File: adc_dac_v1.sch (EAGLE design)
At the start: 349 parts, among them IC1 OPA1662, IC2 ADA4610-2, IC3 ADA4610-2, IC4 OPA1662, IC5 ADA4610-2, IC6 OPA1662, IC7 ADA4610-2, IC8 OPA1662, J1 PJ-202AH, J2 PJ-002B, J3 2-406541-3, P1 M-2X06-87759_M, P2 M-2X10-87759_M, Q1 MMBF4117, U1 AD7960BCPZ-RL7, U10 UA78M05CDCYR, U11 LP5907MFX-1.8/NOPB, U12 ADP2300AUJZ-R7, U13 LM317LIPKG3, U14 LM317LIPKG3, U15 LM337LMX/NOPB, U16 ADR395AUJZ-REEL7, U17 MAX5802, U18 LM337LMX/NOPB, U19 MAX6070BAUT21+T, U2 AD5453, U20 CD40106BM96, U21 ADA4932-1YCPZ-R7, U22 AD7960BCPZ-RL7, U23 BC857BS-13-F, U24 BC857BS-13-F, U25 ADA4932-1YCPZ-R7, U26 AD7960BCPZ-RL7, U27 ADA4932-1YCPZ-R7, U28 AD7960BCPZ-RL7, U29 AD5453YRMZ-REEL7, U3 ADA4932-1YCPZ-R7, U30 AD5453, U31 BC857BS-13-F, U32 AD5453, U33 INA199C2DCKT, U34 INA199C2DCKT, U36 AD8244BRMZ, U4 NLSX3018DTR2G, U5 NLSX3018DTR2G, U6 ADS7952SRHBT, U7 OPA202, U8 REF5025AIDR, U9 ADP150AUJZ-3.3-R7, X1 BU-SMA-G, X2 BU-SMA-G, X3 BU-SMA-G, X4 BU-SMA-G, X5 BU-SMA-G, X6 BU-SMA-G, X7 BU-SMA-G, X8 BU-SMA-G, X9 1365-10

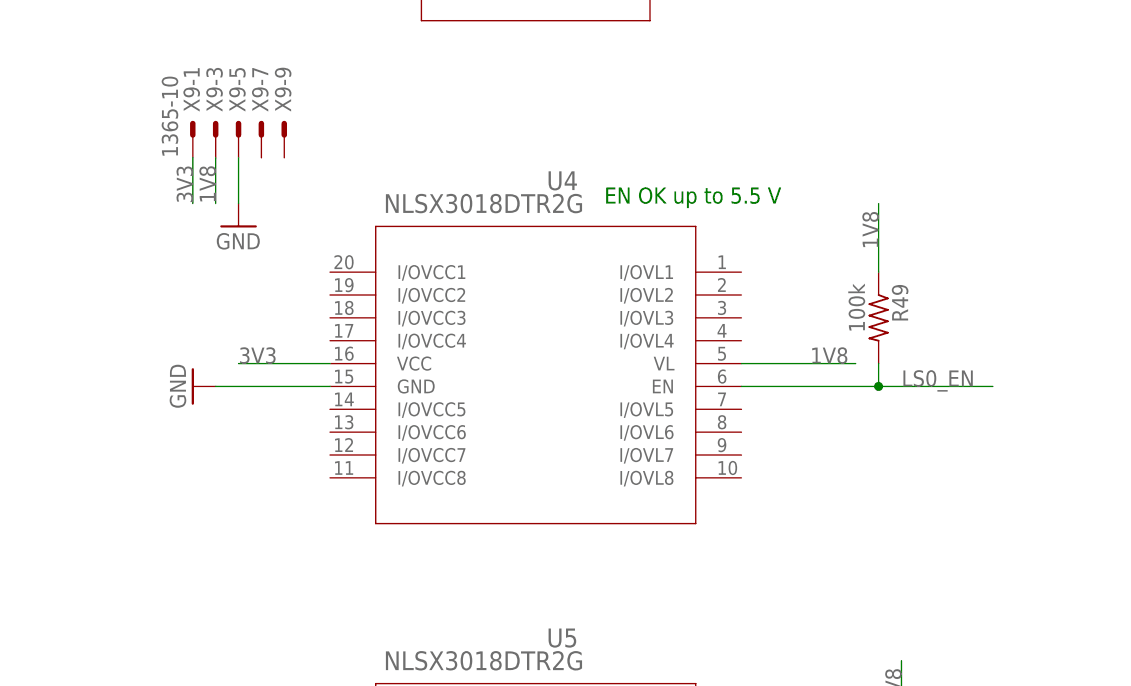
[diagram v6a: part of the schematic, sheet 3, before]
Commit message: placed series terminating resistors
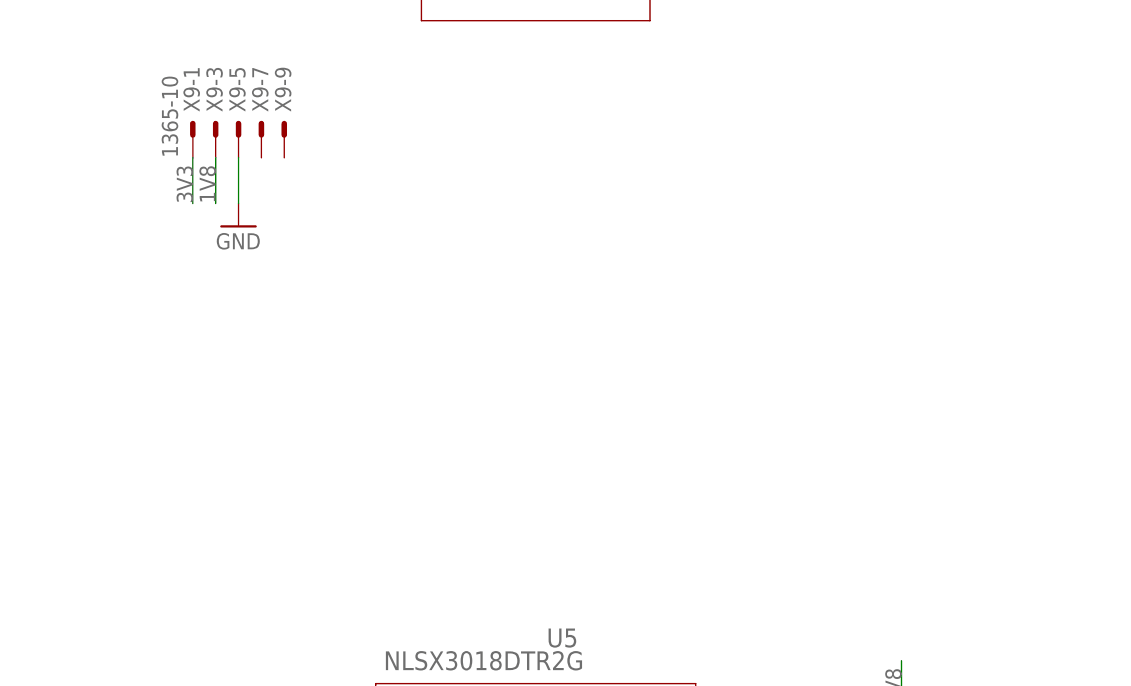
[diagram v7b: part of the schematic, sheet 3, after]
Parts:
- removed R138: 33, rcl:R-US_R0603
- removed R151, R152: DNP, rcl:R-US_R0603
- removed R49: 100k, rcl:R-US_R0603
- removed U4: NLSX3018DTR2G, open_covg:NLSX3018DTR2G
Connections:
- new net N$55: R134.2, U6.SDO
- net 1V8: no longer R49.1, U4.VL
- net 3V3: no longer U4.VCC
- net ADCS_SDO: no longer R134.2, U6.SDO
- net GND: no longer U4.GND
- net LS0_EN: no longer R49.2, U4.EN
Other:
- note removed: "EN OK up to 5.5 V"
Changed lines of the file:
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@@
 <part name="R47" library="rcl" library_urn="urn:adsk.eagle:library:334" deviceset="R-US_" device="R0603" package3d_urn="urn:adsk.eagle:package:23555/3" value="0"/>
 <part name="R48" library="rcl" library_urn="urn:adsk.eagle:library:334" deviceset="R-US_" device="R0603" package3d_urn="urn:adsk.eagle:package:23555/3" value="0"/>
-<part name="GND75" library="supply1" library_urn="urn:adsk.eagle:library:371" deviceset="GND" device=""/>
-<part name="R49" library="rcl" library_urn="urn:adsk.eagle:library:334" deviceset="R-US_" device="R0603" package3d_urn="urn:adsk.eagle:package:23555/3" value="100k"/>
 <part name="R50" library="rcl" library_urn="urn:adsk.eagle:library:334" deviceset="R-US_" device="R0603" package3d_urn="urn:adsk.eagle:package:23555/3" value="100k"/>
 <part name="GND76" library="supply1" library_urn="urn:adsk.eagle:library:371" deviceset="GND" device=""/>
@@
 <part name="U31" library="open_covg" deviceset="HN1A01FU-YLFCT" device="" value="BC857BS-13-F"/>
 <part name="U20" library="open_covg" deviceset="CD40106BM96" device=""/>
-<part name="U4" library="open_covg" deviceset="NLSX3018DTR2G" device=""/>
 <part name="U5" library="open_covg" deviceset="NLSX3018DTR2G" device=""/>
 <part name="U19" library="open_covg" deviceset="MAX6070BAUT21+T" device=""/>
@@
 <part name="R136" library="rcl" library_urn="urn:adsk.eagle:library:334" deviceset="R-US_" device="R0603" package3d_urn="urn:adsk.eagle:package:23555/3" value="33"/>
 <part name="R137" library="rcl" library_urn="urn:adsk.eagle:library:334" deviceset="R-US_" device="R0603" package3d_urn="urn:adsk.eagle:package:23555/3" value="33"/>
-<part name="R138" library="rcl" library_urn="urn:adsk.eagle:library:334" deviceset="R-US_" device="R0603" package3d_urn="urn:adsk.eagle:package:23555/3" value="33"/>
 <part name="R139" library="rcl" library_urn="urn:adsk.eagle:library:334" deviceset="R-US_" device="R0603" package3d_urn="urn:adsk.eagle:package:23555/3" value="33"/>
 <part name="R140" library="rcl" library_urn="urn:adsk.eagle:library:334" deviceset="R-US_" device="R0603" package3d_urn="urn:adsk.eagle:package:23555/3" value="33"/>
@@
 <part name="R149" library="rcl" library_urn="urn:adsk.eagle:library:334" deviceset="R-US_" device="R0603" package3d_urn="urn:adsk.eagle:package:23555/3" value="33"/>
 <part name="R150" library="rcl" library_urn="urn:adsk.eagle:library:334" deviceset="R-US_" device="R0603" package3d_urn="urn:adsk.eagle:package:23555/3" value="33"/>
-<part name="R151" library="rcl" library_urn="urn:adsk.eagle:library:334" deviceset="R-US_" device="R0603" package3d_urn="urn:adsk.eagle:package:23555/3" value="DNP"/>
-<part name="R152" library="rcl" library_urn="urn:adsk.eagle:library:334" deviceset="R-US_" device="R0603" package3d_urn="urn:adsk.eagle:package:23555/3" value="DNP"/>
 <part name="R153" library="rcl" library_urn="urn:adsk.eagle:library:334" deviceset="R-US_" device="R0603" package3d_urn="urn:adsk.eagle:package:23555/3" value="4.7k"/>
 <part name="R154" library="rcl" library_urn="urn:adsk.eagle:library:334" deviceset="R-US_" device="R0603" package3d_urn="urn:adsk.eagle:package:23555/3" value="4.7k"/>
@@
 <attribute name="VALUE" x="163.83" y="99.822" size="1.778" layer="96" rot="R180"/>
 </instance>
-<instance part="R138" gate="G$1" x="81.28" y="71.12" smashed="yes" rot="R180">
-<attribute name="NAME" x="85.09" y="69.6214" size="1.778" layer="95" rot="R180"/>
-<attribute name="VALUE" x="85.09" y="74.422" size="1.778" layer="96" rot="R180"/>
-</instance>
-<instance part="R151" gate="G$1" x="152.4" y="40.64" smashed="yes" rot="R90">
-<attribute name="NAME" x="150.9014" y="36.83" size="1.778" layer="95" rot="R90"/>
-<attribute name="VALUE" x="155.702" y="36.83" size="1.778" layer="96" rot="R90"/>
-</instance>
-<instance part="R152" gate="G$1" x="144.78" y="27.94" smashed="yes" rot="R90">
-<attribute name="NAME" x="143.2814" y="24.13" size="1.778" layer="95" rot="R90"/>
-<attribute name="VALUE" x="148.082" y="24.13" size="1.778" layer="96" rot="R90"/>
-</instance>
 </instances>
 <busses>
@@
 <net name="ADCS_SDO" class="0">
 <segment>
-<pinref part="U6" gate="A" pin="SDO"/>
-<wire x1="119.38" y1="101.6" x2="147.32" y2="101.6" width="0.1524" layer="91"/>
-<pinref part="R134" gate="G$1" pin="2"/>
-</segment>
-<segment>
 <wire x1="157.48" y1="101.6" x2="172.72" y2="101.6" width="0.1524" layer="91"/>
 <label x="167.64" y="101.6" size="1.778" layer="95"/>
@@
 <wire x1="165.1" y1="96.52" x2="172.72" y2="96.52" width="0.1524" layer="91"/>
 <label x="167.64" y="96.52" size="1.778" layer="95"/>
+</segment>
+</net>
+<net name="N$55" class="0">
+<segment>
+<pinref part="U6" gate="A" pin="SDO"/>
+<pinref part="R134" gate="G$1" pin="2"/>
+<wire x1="119.38" y1="101.6" x2="147.32" y2="101.6" width="0.1524" layer="91"/>
 </segment>
 </net>
@@
 <sheet>
 <plain>
-<text x="223.52" y="132.08" size="1.778" layer="91">EN OK up to 5.5 V</text>
 <text x="223.52" y="193.04" size="1.778" layer="91">VSS - VDD
 to FET switches on analog board</text>
@@
 <attribute name="DRAWING_NAME" x="190.5" y="19.05" size="2.54" layer="94"/>
 </instance>
-<instance part="GND75" gate="1" x="177.8" y="111.76" smashed="yes" rot="R270">
-<attribute name="VALUE" x="175.26" y="114.3" size="1.778" layer="96" rot="R270"/>
-</instance>
-<instance part="R49" gate="G$1" x="254" y="119.38" smashed="yes" rot="R270">
-<attribute name="NAME" x="255.4986" y="123.19" size="1.778" layer="95" rot="R270"/>
-<attribute name="VALUE" x="250.698" y="123.19" size="1.778" layer="96" rot="R270"/>
-</instance>
 <instance part="R50" gate="G$1" x="256.54" y="68.58" smashed="yes" rot="R270">
 <attribute name="NAME" x="258.0386" y="72.39" size="1.778" layer="95" rot="R270"/>
@@
 <attribute name="NAME" x="211.1756" y="189.4586" size="2.0828" layer="95" ratio="6" rot="SR0"/>
 <attribute name="VALUE" x="210.5406" y="186.9186" size="2.0828" layer="96" ratio="6" rot="SR0"/>
-</instance>
-<instance part="U4" gate="A" x="241.3" y="124.46" smashed="yes" rot="MR0">
-<attribute name="NAME" x="220.6244" y="133.5786" size="2.0828" layer="95" ratio="6" rot="SMR0"/>
-<attribute name="VALUE" x="221.2594" y="131.0386" size="2.0828" layer="96" ratio="6" rot="SMR0"/>
 </instance>
 <instance part="U5" gate="A" x="241.3" y="73.66" smashed="yes" rot="MR0">
@@
 <nets>
 <net name="1V8" class="1">
-<segment>
-<wire x1="238.76" y1="114.3" x2="251.46" y2="114.3" width="0.1524" layer="91"/>
-<label x="246.38" y="114.3" size="1.778" layer="95"/>
-<pinref part="U4" gate="A" pin="VL"/>
-</segment>
-<segment>
-<pinref part="R49" gate="G$1" pin="1"/>
-<wire x1="254" y1="124.46" x2="254" y2="132.08" width="0.1524" layer="91"/>
-<label x="254" y="127" size="1.778" layer="95" rot="R90"/>
-</segment>
 <segment>
 <wire x1="238.76" y1="63.5" x2="251.46" y2="63.5" width="0.1524" layer="91"/>
@@
 <net name="3V3" class="1">
 <segment>
-<wire x1="193.04" y1="114.3" x2="182.88" y2="114.3" width="0.1524" layer="91"/>
-<label x="182.88" y="114.3" size="1.778" layer="95"/>
-<pinref part="U4" gate="A" pin="VCC"/>
-</segment>
-<segment>
 <wire x1="193.04" y1="63.5" x2="182.88" y2="63.5" width="0.1524" layer="91"/>
 <label x="182.88" y="63.5" size="1.778" layer="95"/>
@@
 </net>
 <net name="GND" class="1">
-<segment>
-<pinref part="GND75" gate="1" pin="GND"/>
-<wire x1="180.34" y1="111.76" x2="193.04" y2="111.76" width="0.1524" layer="91"/>
-<pinref part="U4" gate="A" pin="GND"/>
-</segment>
 <segment>
 <pinref part="GND76" gate="1" pin="GND"/>
@@
 </segment>
 </net>
-<net name="LS0_EN" class="0">
-<segment>
-<wire x1="238.76" y1="111.76" x2="254" y2="111.76" width="0.1524" layer="91"/>
-<pinref part="R49" gate="G$1" pin="2"/>
-<wire x1="254" y1="114.3" x2="254" y2="111.76" width="0.1524" layer="91"/>
-<wire x1="254" y1="111.76" x2="266.7" y2="111.76" width="0.1524" layer="91"/>
-<junction x="254" y="111.76"/>
-<label x="256.54" y="111.76" size="1.778" layer="95"/>
-<pinref part="U4" gate="A" pin="EN"/>
-</segment>
-</net>

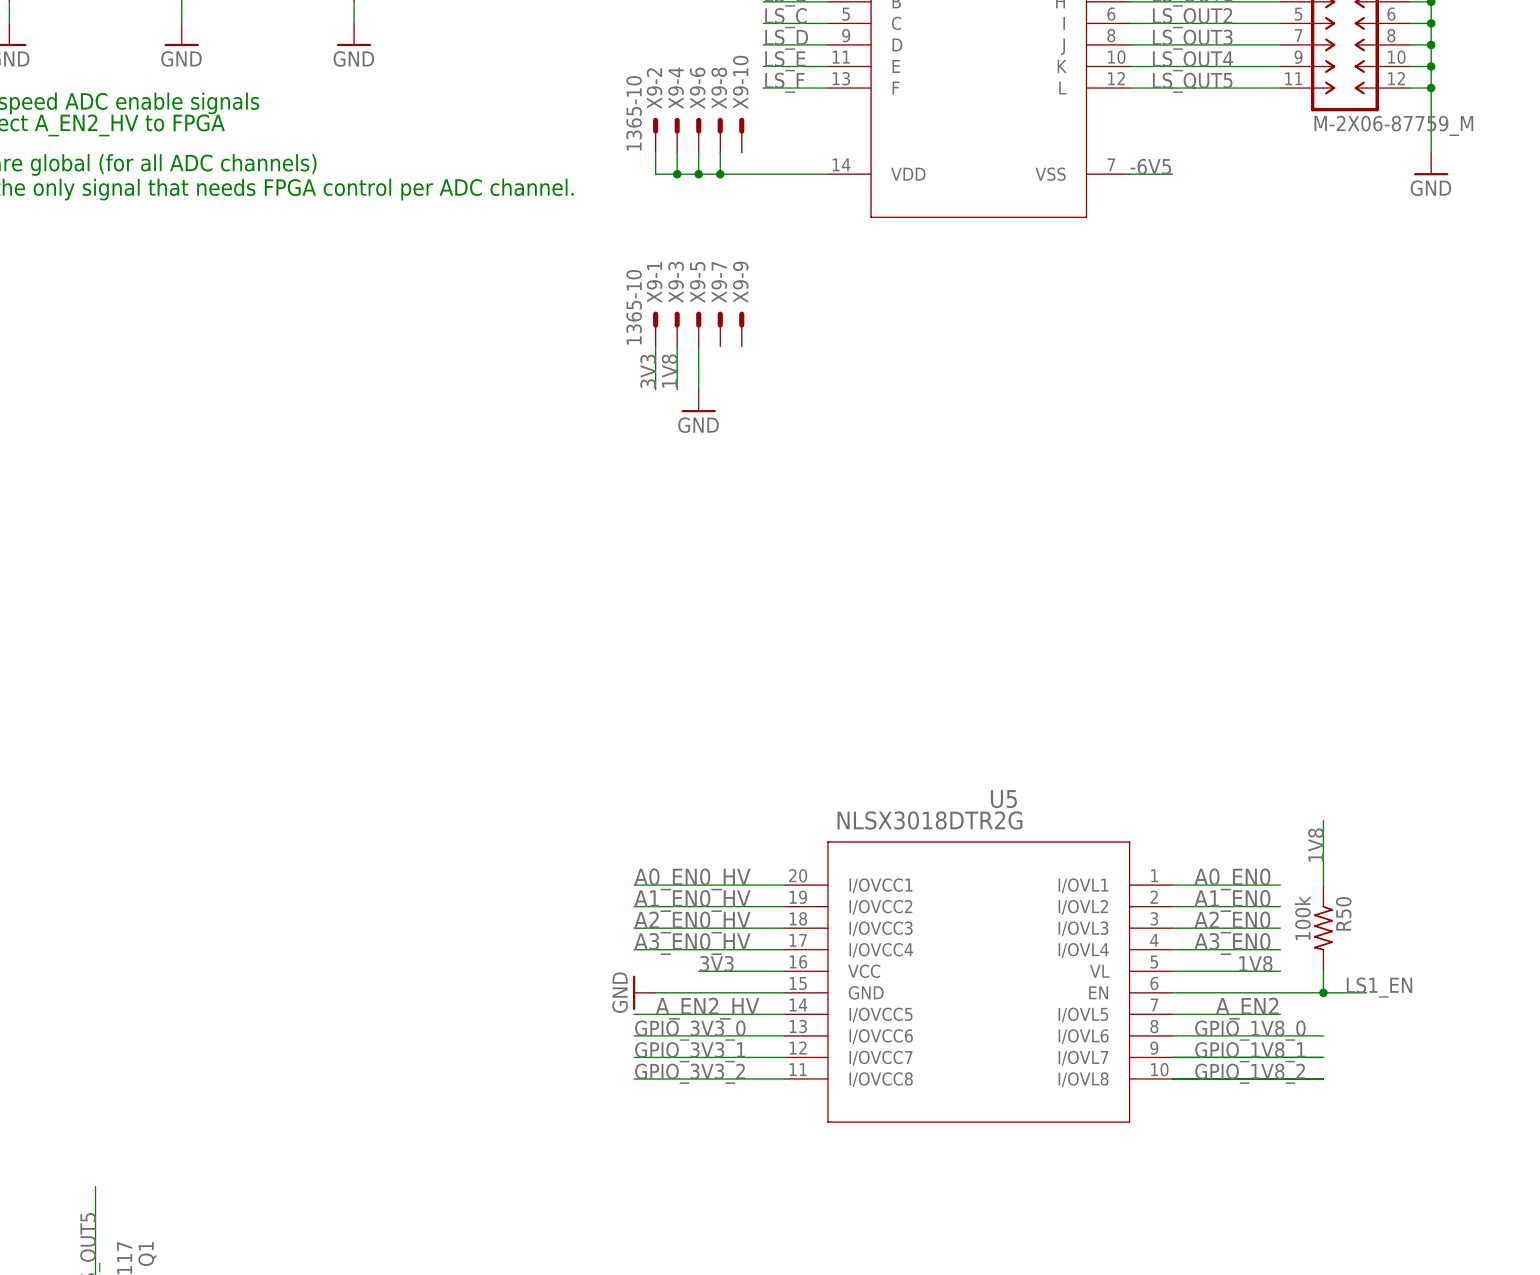
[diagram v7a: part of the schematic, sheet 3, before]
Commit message: cleared PCB DRC errors
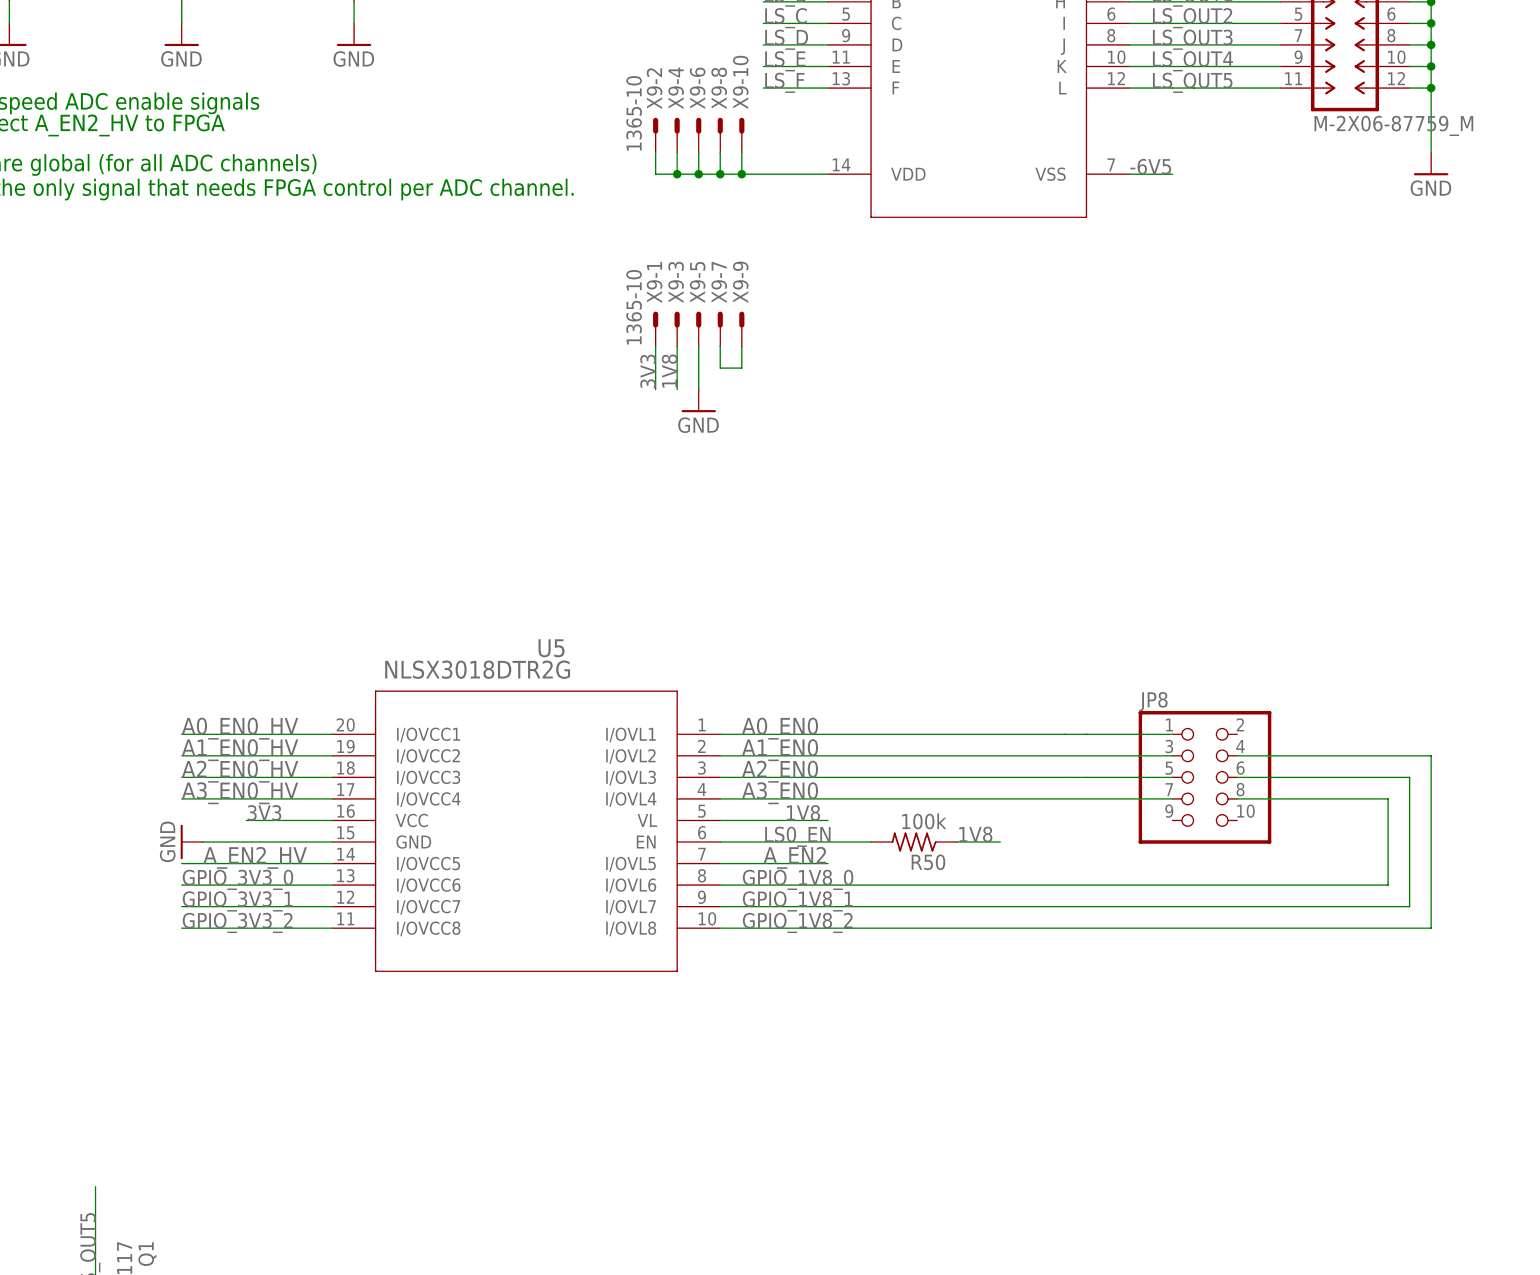
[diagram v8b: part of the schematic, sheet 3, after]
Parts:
- added JP8: (no value), pinhead-2:PINHD-2X05_2.54-SMD
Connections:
- removed net A2_IN_BUF-: C76.1, R81.1, R84.2, R86.2
- removed net JP1-2: OK1JP1_EVEN.DGND_2
- removed net JP1-53: OK1JP1_ODD.B8-L6P_0
- removed net JP1-78: OK1JP1_EVEN.DGND_78
- removed net JP1-80: OK1JP1_EVEN.DGND_80
- removed net JP2-1: OK1JP2_ODD.DGND_1
- removed net JP2-12: OK1JP2_EVEN.NC_12
- removed net JP2-13: OK1JP2_ODD.DGND_13
- removed net JP2-14: OK1JP2_EVEN.DGND_14
- removed net JP2-3: OK1JP2_ODD.NC_3
- removed net JP2-36: OK1JP2_EVEN.DGND_36
- removed net JP2-56: OK1JP2_EVEN.DGND_56
- removed net JP2-78: OK1JP2_EVEN.DGND_78
- removed net JP2-80: OK1JP2_EVEN.DGND_80
- removed net LS1_EN: OK1JP1_EVEN.USB_SCL, R50.2, U5.EN
- new net JP1-10: OK1JP1_EVEN.USB_SCL
- net A0_EN0: now also JP8.1; no longer OK1JP1_EVEN.D9-L7P_0
- net A0_EN0_HV: now also OK1JP1_EVEN.D9-L7P_0
- net A1_EN0: now also JP8.3; no longer OK1JP1_ODD.A8-L6N_0
- net A1_EN0_HV: now also OK1JP1_ODD.A8-L6N_0
- net A2_EN0: now also JP8.5; no longer OK1JP1_EVEN.B16-L63P_0
- net A2_EN0_HV: now also OK1JP1_EVEN.B16-L63P_0
- net A2_IN-_BUF: now also C76.1, R81.1, R84.2, R86.2
- net A3_EN0: now also JP8.7; no longer OK1JP1_EVEN.A16-L63N_0
- net A3_EN0_HV: now also OK1JP1_EVEN.A16-L63N_0, OK1JP1_ODD.B8-L6P_0
- net D1_CSB_T: now also R139.2
- net GND: now also OK1JP1_EVEN.DGND_2, OK1JP1_EVEN.DGND_78, OK1JP1_EVEN.DGND_80, OK1JP2_EVEN.DGND_14, OK1JP2_EVEN.DGND_36, OK1JP2_EVEN.DGND_56, OK1JP2_EVEN.DGND_78, OK1JP2_EVEN.DGND_80, OK1JP2_ODD.DGND_1, OK1JP2_ODD.DGND_13; no longer JP7.6
- net GPIO_1V8_0: now also JP8.8
- net GPIO_1V8_1: now also JP8.6
- net GPIO_1V8_2: now also JP8.4
- net GP_ADC3: now also JP7.6
- net LS0_EN: now also R50.2, U5.EN
- net N$33: now also X9-10.S
- net N$54: now also X9-7.S, X9-9.S; no longer R139.2
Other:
- moved on the sheet: R50, U5
